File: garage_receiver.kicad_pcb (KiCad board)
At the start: 2 copper layers, 85 x 45 mm, 25 parts, among them J1 Conn_01x04_Female, J2 Screw_Terminal_01x04, Q1 2N7002, SW1 SW_DIP_x08, U1 HT12D, U2 MP1470

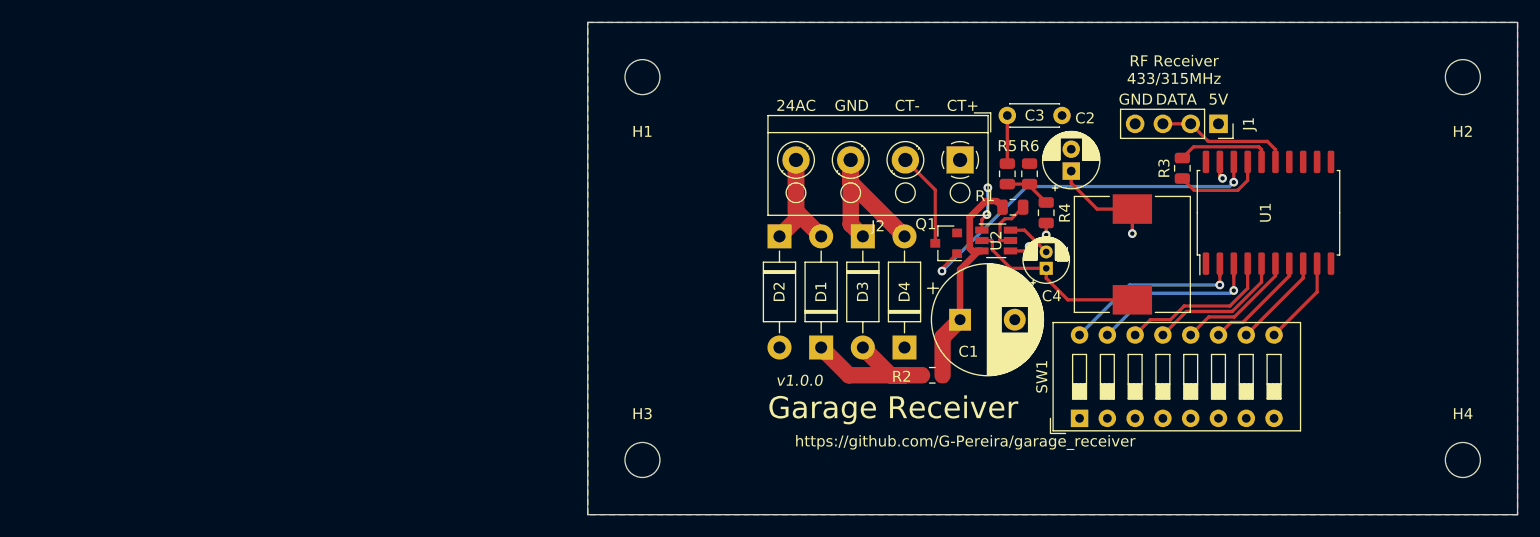
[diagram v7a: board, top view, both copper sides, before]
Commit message: DC/DC converter updated to input range 4V to 48V
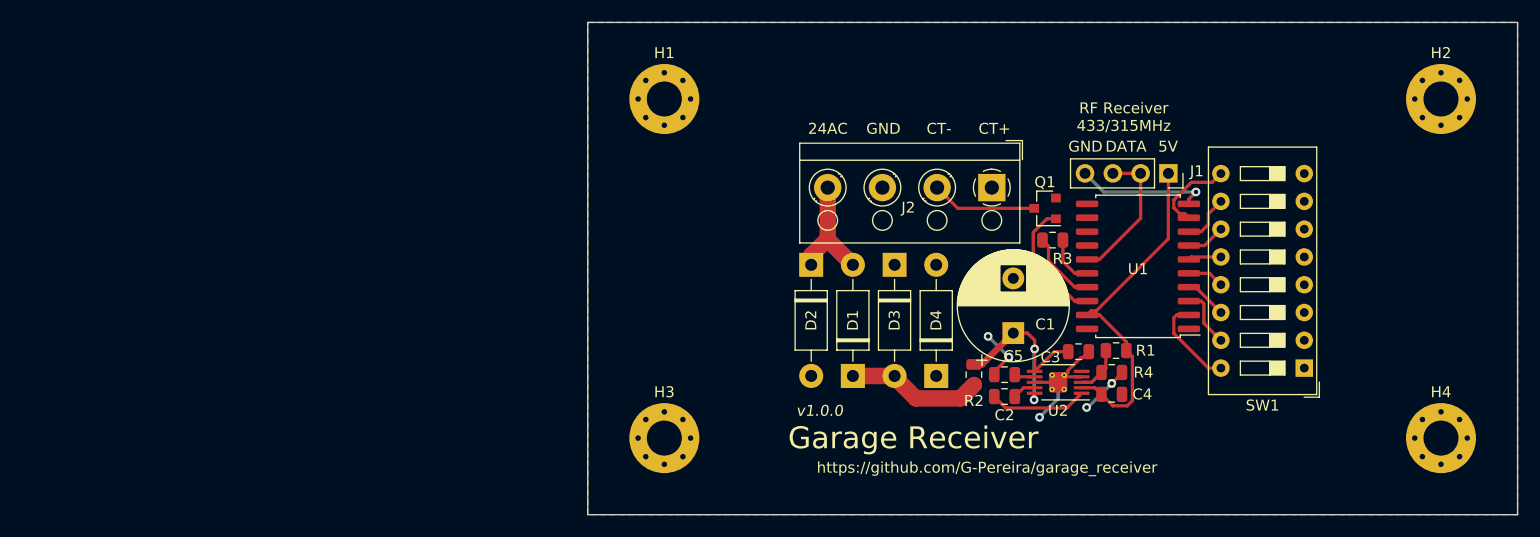
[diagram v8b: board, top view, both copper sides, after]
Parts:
- removed L1: 33u, Inductor_SMD:L_10.4x10.4_H4.8
- removed R5: 10k, Resistor_SMD:R_0805_2012Metric
- removed R6: 2k, Resistor_SMD:R_0805_2012Metric
- added C5: 100n, Capacitor_SMD:C_0805_2012Metric, F.Cu at (211.6, 109.4)
- C2: value 47u -> 1u; footprint Capacitor_THT:CP_Radial_D5.0mm_P2.00mm -> Capacitor_SMD:C_0805_2012Metric
- C3: value 2.2u -> 1u; footprint Capacitor_THT:C_Disc_D4.3mm_W1.9mm_P5.00mm -> Capacitor_SMD:C_0805_2012Metric
- C4: value 1u -> 10u; footprint Capacitor_THT:CP_Radial_D4.0mm_P1.50mm -> Capacitor_SMD:C_0805_2012Metric
- H1, H2, H3, H4: footprint MountingHole:MountingHole_3.2mm_M3 -> MountingHole:MountingHole_3.2mm_M3_Pad_Via
- R1: value 100k -> 62k
- R4: value 100k -> 20k
- U2: value MP1470 -> LTC3255; footprint Package_TO_SOT_SMD:TSOT-23-6 -> Package_SO:MSOP-10-1EP_3x3mm_P0.5mm_EP1.68x1.88mm_ThermalVias
- moved C3 22.6 mm to (218.3, 107.3)
- moved C2 21.5 mm to (211.6, 111.4), turned to 0 degrees
- moved SW1 21.0 mm to (239.0, 108.8), turned to 180 degrees
- moved R1 16.2 mm to (221.8, 107.2), turned to 180 degrees
- moved R4 15.8 mm to (221.4, 109.2), turned to 0 degrees
- moved U2 14.1 mm to (216.5, 110.1), turned to 180 degrees
- moved R3 13.6 mm to (216.0, 97.1), turned to 0 degrees
- moved C4 13.0 mm to (221.4, 111.2), turned to 0 degrees
- moved U1 12.9 mm to (223.8, 99.5), turned to 180 degrees
- moved Q1 9.58 mm to (215.3, 94.2)
- moved J1 6.44 mm to (226.6, 91.0)
- moved C1 5.02 mm to (212.4, 105.6), turned to 90 degrees
- moved D4 3.89 mm to (205.3, 109.5)
- moved D3 3.89 mm to (201.5, 99.4)
- moved D1 3.89 mm to (197.7, 109.5)
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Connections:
- C1 pad 1: +12V -> +36V
- C2 pad 1: +5V -> Net-(C2-Pad1)
- C2 pad 2: GND -> Net-(C2-Pad2)
- C3 pad 1: +5V -> +36V
- C4 pad 1: Net-(C4-Pad1) -> +5V
- C4 pad 2: Net-(C4-Pad2) -> GND
- R1 pad 1: +12V -> +5V
- R2 pad 1: +12V -> +36V
- R4 pad 1: Net-(R4-Pad1) -> Net-(R1-Pad2)
- R4 pad 2: Net-(R4-Pad2) -> GND
- U2 pad 1: GND -> Net-(C2-Pad1)
- U2 pad 2: Net-(C4-Pad1) -> +5V
- U2 pad 3: +12V -> Net-(R1-Pad2)
- U2 pad 4: Net-(R4-Pad2) -> GND
- U2 pad 5: Net-(R1-Pad2) -> Net-(U2-Pad5)
- U2 pad 6: Net-(C4-Pad2) -> +36V
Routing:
- net GND: track 4.48 -> 34.5 mm, vias 2 -> 6
- net /open: track 34.1 -> 11.6 mm, vias 2 -> 0
- net +12V: track 20.9 -> 0.00 mm
- net +36V: track 0.00 -> 19.0 mm, vias 0 -> 2
- net Net-(C4-Pad1): track 17.0 -> 0.00 mm
- net GNDPWR: track 16.5 -> 0.00 mm
- net +5V: track 16.8 -> 32.2 mm, vias 2 -> 0
- net Net-(SW1-Pad15): track 16.8 -> 5.46 mm, vias 1 -> 0
- net Net-(SW1-Pad14): track 14.3 -> 3.89 mm
- net Net-(SW1-Pad13): track 12.7 -> 3.36 mm
- net Net-(SW1-Pad16): track 17.7 -> 8.53 mm, vias 1 -> 0
- net Net-(C2-Pad1): track 0.00 -> 8.98 mm
- net Net-(SW1-Pad12): track 11.1 -> 3.02 mm
- net Net-(SW1-Pad11): track 9.84 -> 3.55 mm
- net Net-(R4-Pad2): track 4.96 -> 0.00 mm, vias 2 -> 0
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- added copper zone on B.Cu, net GNDPWR
- removed copper zone on B.Cu, net +5V
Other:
- net class 12V removed
- net class 36V added: clearance 0.2, trace_width 0.6, via_dia 0.8, via_drill 0.4
